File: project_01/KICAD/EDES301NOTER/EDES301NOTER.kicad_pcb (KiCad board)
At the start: 2 copper layers, 34 parts, among them Q1 S8050, Q2 BSS84, Q3 BSS84, Q4 BSS84, Q5 BSS138, Q7 BSS138, U1 POCKETBEAGLE, U3 TPS613222ADBVR

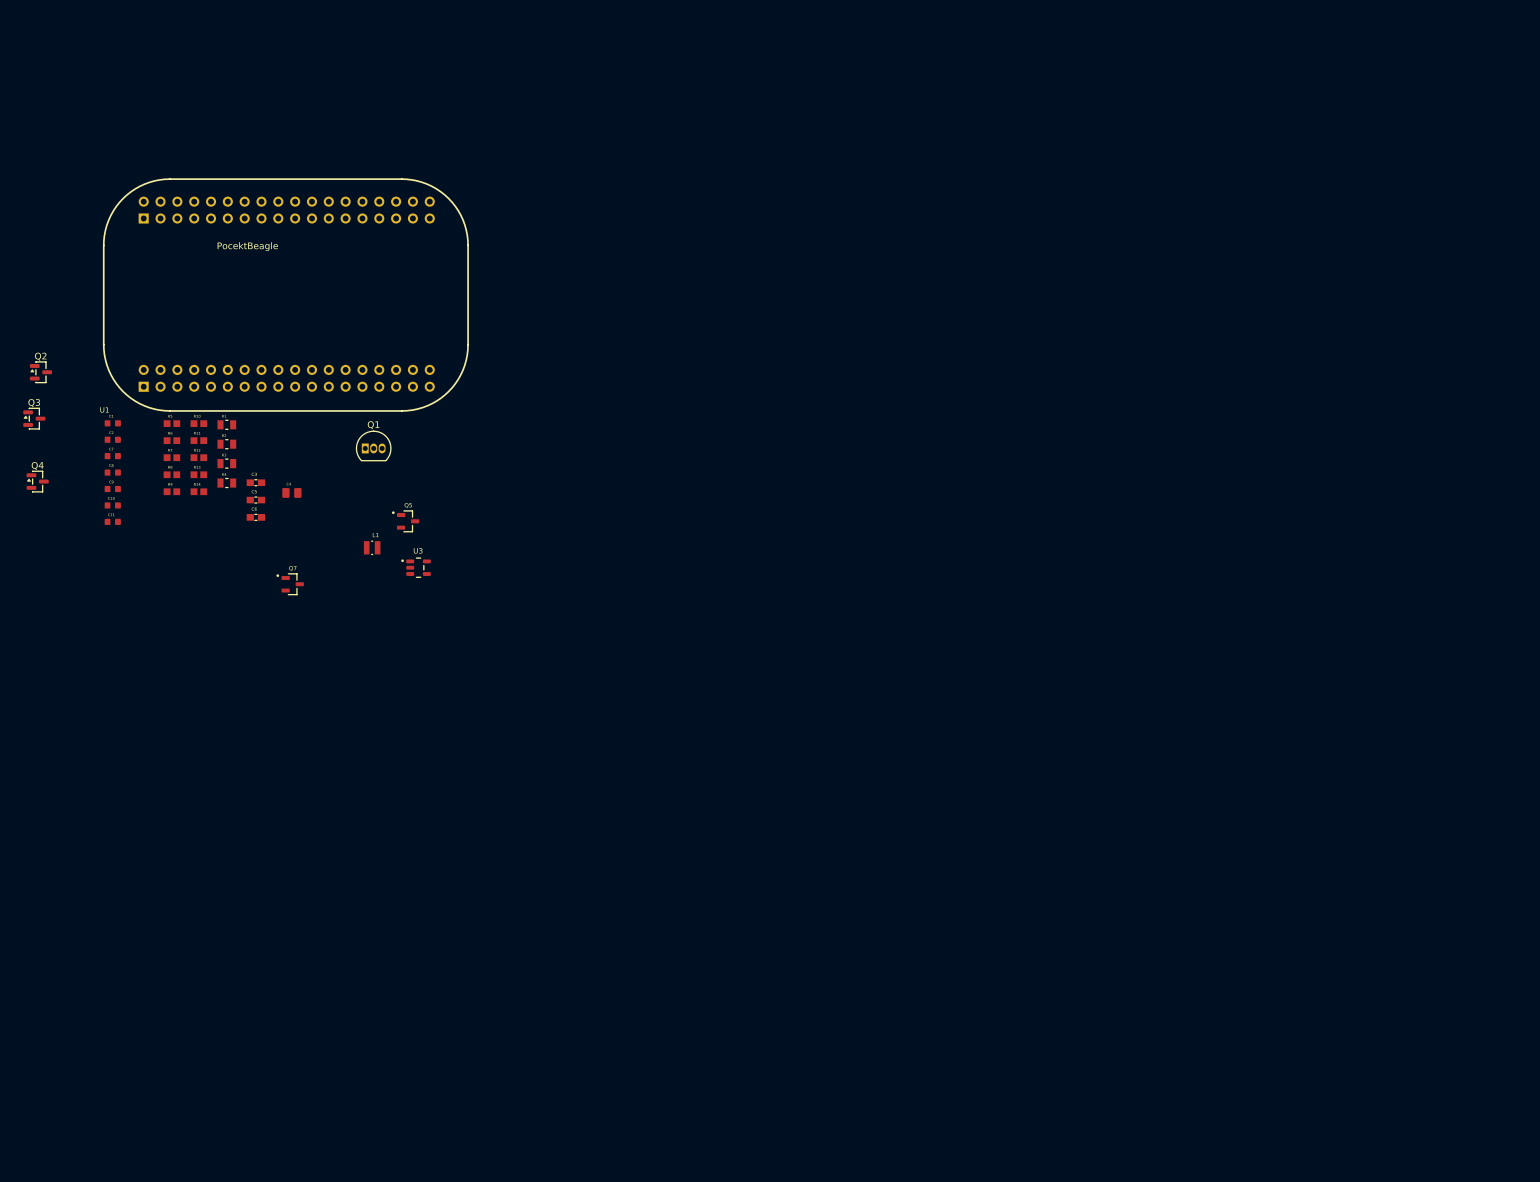
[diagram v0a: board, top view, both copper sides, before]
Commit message: SoftwareWork
Upload software flow diagram as well as did some work to understand interacting with my devices hardware.
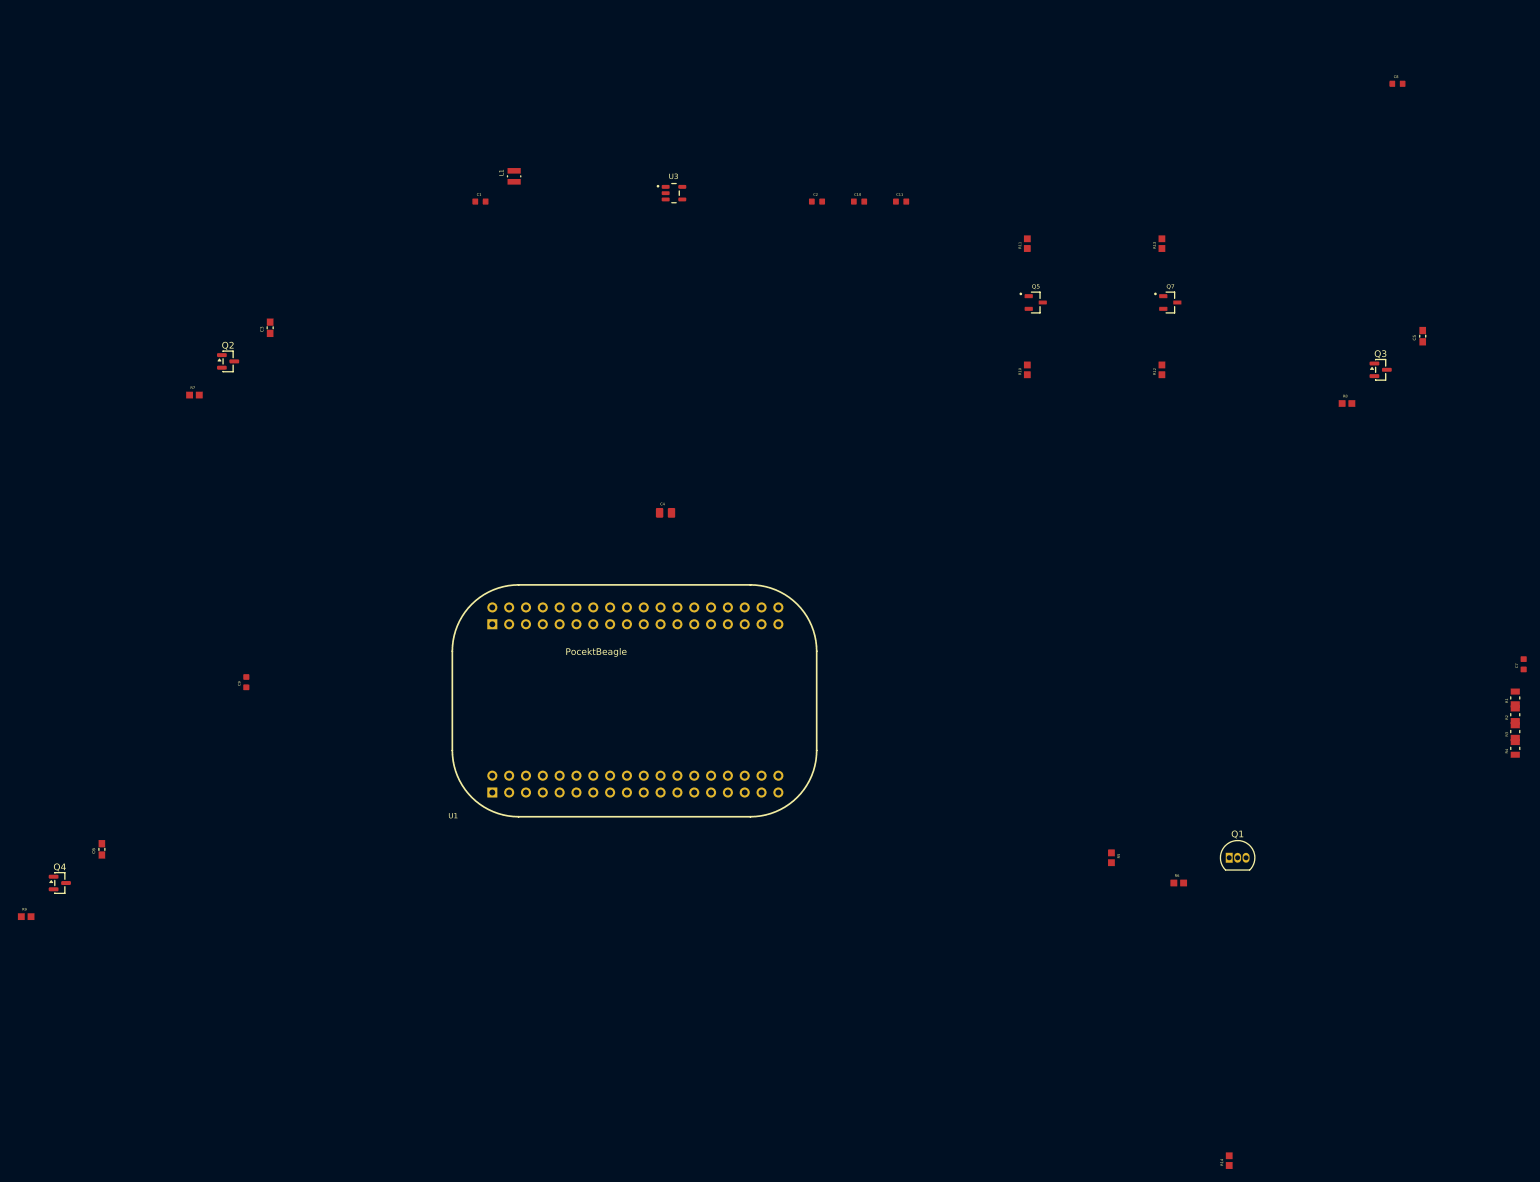
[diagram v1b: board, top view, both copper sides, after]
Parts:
- moved C7 215.3 mm to (290.8, 132.1), turned to 90 degrees
- moved Q3 203.4 mm to (269.2, 87.6)
- moved C8 202.6 mm to (271.8, 44.5)
- moved R1 198.8 mm to (289.6, 137.2), turned to 90 degrees
- moved R2 198.7 mm to (289.6, 139.7), turned to 90 degrees
- moved R3 198.7 mm to (289.6, 142.2), turned to 90 degrees
- moved R4 198.6 mm to (289.6, 144.8), turned to 90 degrees
- moved R14 185.4 mm to (246.4, 207.0), turned to 90 degrees
- moved C5 177.9 mm to (275.6, 82.5), turned to 90 degrees
- moved R8 177.7 mm to (264.2, 92.7)
- moved R6 166.0 mm to (238.8, 165.1)
- moved R5 156.2 mm to (228.6, 161.3), turned to -90 degrees
- moved R13 149.5 mm to (236.2, 68.6), turned to 90 degrees
- moved R12 146.0 mm to (236.2, 87.6), turned to 90 degrees
- moved Q1 144.3 mm to (246.4, 161.3)
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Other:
- board text added: "Main Sheet"

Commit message: SchemV2.2
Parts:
- added C12: 1uF, Footprints:CAPC1608X90N, F.Cu at (147.0, 57.8)
- added C13: 1uF, Footprints:CAPC1608X90N, F.Cu at (147.0, 60.3)
- added C14: 1uF, Footprints:CAPC1608X90N, F.Cu at (64.0, 121.8)
- added C15: 4.7uF, Footprints:CAPC1608X90N, F.Cu at (64.0, 124.3)
- added C16: 1uF, Footprints:CAPC1608X90N, F.Cu at (64.0, 126.8)
- added C17: 1uF, Footprints:CAPC1608X90N, F.Cu at (64.0, 129.3)
- added C18: 4.7uF, Footprints:CAPC1608X90N, F.Cu at (64.0, 131.8)
- added C19: 1uF, Footprints:CAPC1608X90N, F.Cu at (68.0, 119.4)
- added C20: 1uF, Footprints:CAPC1608X90N, F.Cu at (68.0, 121.8)
- added C21: 1uF, Footprints:CAPC1608X90N, F.Cu at (68.0, 124.3)
- added C22: 1uF, Footprints:CAPC1608X90N, F.Cu at (68.0, 126.8)
- added D1: B0530W-7-F, B0530W-7-F:SOD3715X145N, F.Cu at (152.2, 59.0)
- added D2: B0530W-7-F, B0530W-7-F:SOD3715X145N, F.Cu at (73.1, 119.8)
- added D3: B0530W-7-F, B0530W-7-F:SOD3715X145N, F.Cu at (73.1, 123.0)
- added D4: B0530W-7-F, B0530W-7-F:SOD3715X145N, F.Cu at (73.1, 126.3)
- added J1: FH12-24S-0.5SH55, CF4224FH0R0-05-NH:CONN24X1_FH12-24S-0.5SH55_HIR, F.Cu at (73.8, 110.6)
- added L2: 47uH, IFSC2020DEER470M01:IND_IFSC-2020DE-01_VIS, F.Cu at (80.9, 122.1)
- added Q6: BSS84, Package_TO_SOT_SMD:SOT-23, F.Cu at (151.6, 51.1)
- added R15: 100k, Footprints:RESC1607X60N, F.Cu at (147.1, 52.7)
- added R16: 100k, Footprints:RESC1607X60N, F.Cu at (147.1, 55.3)
- added R17: 1M, Footprints:RESC1607X60N, F.Cu at (78.2, 129.8)
- added R18: 2.2, Footprints:RESC1607X60N, F.Cu at (78.2, 132.4)
- added RT1: NXRT15XH103FA1B040, HomeBrew:2_Wire_Connector, F.Cu at (90.7, 89.0)
- added U2: DRV5032FCDBZR, DRV5032FCDBZR:DBZ0003A-IPC_A, F.Cu at (151.5, 55.3)
- added U4: ~, HomeBrew:4_Wire_Connector, F.Cu at (157.5, 94.4)
- added U5: ~, FH34SRJ-18S-0.5SH:CONN18x1_FH34SRJ-18S-0.5SH50_HIR, F.Cu at (130.0, 103.5)
- added U7: PMF250XNEX, PMF250XNEX:PMF250XNEX_NEX, F.Cu at (82.1, 128.3)
- C4: value C -> 47uF
- U1: footprint POCKETBEAGLE:POCKETBEAGLE -> POCKETBEAGLE (1):POCKETBEAGLE
- moved R14 185.7 mm to (147.1, 50.1), turned to 0 degrees
- moved R1 168.6 mm to (123.5, 107.7), turned to 0 degrees
- moved R2 168.5 mm to (123.5, 110.6), turned to 0 degrees
- moved R3 168.5 mm to (123.5, 113.5), turned to 0 degrees
- moved R4 168.4 mm to (123.5, 116.5), turned to 0 degrees
- moved C7 155.0 mm to (136.7, 115.9), turned to 0 degrees
- moved C5 142.1 mm to (136.9, 113.3), turned to 0 degrees
- moved Q3 139.6 mm to (132.2, 114.2)
- moved R8 137.8 mm to (127.8, 112.6)
- moved Q1 125.8 mm to (131.8, 109.5)
- moved R6 123.9 mm to (127.8, 110.1)
- moved C8 121.3 mm to (162.5, 97.0)
- moved R5 114.3 mm to (127.8, 107.5), turned to 0 degrees
- moved U1 109.8 mm to (119.4, 45.6), turned to 180 degrees
- moved R13 90.7 mm to (153.1, 104.8), turned to 0 degrees
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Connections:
- net /PWM_BL_CTR renamed Net-(Q1-B)
- net Net-(U1-AIN6/GPIO87) renamed /TFT_D/C
- net Net-(U1-GPIO23) renamed /TFT_RST
- net Net-(U1-GPIO26) renamed /EPPR_BUSY
- net Net-(U1-GPIO45) renamed /EPPR_RST
- C1 pad 1: +3.3VA -> Net-(Q2-D)
- C10 pad 1: /+5V -> +5V
- C11 pad 1: /+5V -> +5V
- C2 pad 1: /+5V -> +5V
- C3 pad 1: +3.3VA -> Net-(Q2-D)
- C4 pad 1: +3.3VA -> -BATT
- C4 pad 2: Net-(U1-3.3V@2) -> +3.3V
- C5 pad 1: +3.3VA -> Net-(Q3-D)
- C6 pad 1: +3.3VA -> /ePaper Support Circuit/VCI
- C7 pad 2: +3.3VA -> Net-(Q3-D)
- C8 pad 1: -BATT -> +5V
- C8 pad 2: /+5V -> -BATT
- C9 pad 1: -BATT -> /ePaper Support Circuit/PREVGH
- C9 pad 2: +3.3VA -> -BATT
- L1 pad 1: +3.3VA -> Net-(Q2-D)
- Q2 pad 1: Net-(Q2-G) -> /5V Boost Converter/BOOST_PWR
- Q2 pad 2: +3.3VA -> +3.3V
- Q2 pad 3: +3.3VA -> Net-(Q2-D)
- Q3 pad 1: Net-(Q3-G) -> /TFT Display/TFT_BL
- Q3 pad 2: +3.3VA -> +3.3V
- Q3 pad 3: +3.3VA -> Net-(Q3-D)
- Q4 pad 1: Net-(Q4-G) -> /ePaper Support Circuit/EPPR_PWR
- Q4 pad 2: +3.3VA -> +3.3V
- Q4 pad 3: +3.3VA -> /ePaper Support Circuit/VCI
- Q5 pad 1: +3.3VA -> +3.3V
- Q5 pad 2: /DATA -> /CardKB/CARD_SCL
- Q5 pad 3: /DATA -> /CardKB/DATA
- Q7 pad 1: +3.3VA -> +3.3V
- Q7 pad 2: /DATA -> /CardKB/CARD_SDA
- Q7 pad 3: Net-(Q7-D) -> /CardKB/DATA
- R10 pad 1: +3.3VA -> +3.3V
- R10 pad 2: /DATA -> /CardKB/CARD_SCL
- R11 pad 1: /+5V -> +5V
- R11 pad 2: /DATA -> /CardKB/DATA
- R12 pad 1: +3.3VA -> +3.3V
- R12 pad 2: /DATA -> /CardKB/CARD_SDA
- R13 pad 1: /+5V -> +5V
- R13 pad 2: Net-(Q7-D) -> /CardKB/DATA
- R14 pad 1: Net-(U1-GPIO59) -> +3.3V
- R14 pad 2: +3.3V -> /Hall Effect Power Switch/PB_LID
- R5 pad 2: Net-(U1-PWM1A) -> /TFT Display/TFT_BL
- R7 pad 1: Net-(Q2-G) -> /5V Boost Converter/BOOST_PWR
- R7 pad 2: +3.3VA -> +3.3V
- R8 pad 1: Net-(Q3-G) -> /TFT Display/TFT_BL
- R8 pad 2: +3.3VA -> +3.3V
- R9 pad 1: Net-(Q4-G) -> /ePaper Support Circuit/EPPR_PWR
- R9 pad 2: +3.3VA -> +3.3V
- U1 pad 10: /DATA -> /TFT_SDO
- U1 pad 12: /DATA -> /TFT_SDA
- U1 pad 14: +3.3VA -> unconnected-(U1-3.3V@1-Pad14)
- U1 pad 20: Net-(Q3-G) -> /TFT_PWR
- U1 pad 22: -BATT -> unconnected-(U1-GND@3-Pad22)
- U1 pad 37: Net-(U1-PWM1A) -> /TFT_BL
- U1 pad 38: Net-(U1-GPIO59) -> unconnected-(U1-GPIO59-Pad38)
- U1 pad 44: Net-(Q2-G) -> unconnected-(U1-GPIO60-Pad44)
- U1 pad 45: /DATA -> /CARD_SCL
- U1 pad 47: /DATA -> /CARD_SDA
- U1 pad 48: unconnected-(U1-PWR.BTN-Pad48) -> /PB_PWR
- U1 pad 52: Net-(U1-BAT.TEMP) -> /BATT_TEMP
- U1 pad 53: Net-(U1-GPIO65) -> unconnected-(U1-GPIO65-Pad53)
- U1 pad 54: unconnected-(U1-GPIO47-Pad54) -> /EPPR_D/C
- U1 pad 55: unconnected-(U1-GPIO27-Pad55) -> /PB_LID
- U1 pad 56: Net-(Q4-G) -> unconnected-(U1-GPIO64-Pad56)
- U1 pad 58: unconnected-(U1-GPIO46-Pad58) -> /EPPR_PWR
- U1 pad 59: Net-(U1-3.3V@2) -> +3.3V
- U1 pad 6: /DATA -> /TFT_CSX
- U1 pad 60: unconnected-(U1-GPIO44-Pad60) -> /BOOST_PWR
- U1 pad 61: /DATA -> /EPPR_MISO
- U1 pad 65: /DATA -> /EPPR_CLK
- U1 pad 67: /DATA -> /EPPR_CS
- U1 pad 8: /DATA -> /TFT_SDL
- U3 pad 4: /+5V -> +5V
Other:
- board text removed: "Main Sheet"
